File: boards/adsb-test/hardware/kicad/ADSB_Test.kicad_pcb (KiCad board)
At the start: 4 copper layers, 180.9 x 116 mm, 500 parts, among them J1001 Dev USB-C, J1101 USB-A (SDR hub), J1201 SMA GNSS (active antenna), J1301 LCD FPC 30p 0.5mm, J1302 Touch FPC 6p 0.5mm, J1401 m1421 JTAG (J-Link), J1402 ADSBee 1421 Dev Kit, J1403 SMA 1090/978, J1501 microSD (push-pull, detect), J1601 Kingst LA5016 (2x20 keyed), J1801 RP2040 GPIO (pins DNP), J1802 RP2040 SWD, J301 2S Li-ion pack (BAT+, GND, NT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, J601 U.FL Wi-Fi (from module IPEX), J602 RP-SMA Wi-Fi 2.4/5 GHz, J801 HR911105A, J901 User USB-C (PD sink + UART), Q1501 AO3401A, Q1701 MMBT3904, Q1702 MMBT3904, Q1703 MMBT3904, Q1704 MMBT3904, Q201 FDS9435A, SW1801 BOOTSEL (programmer), SW401 POWER (slide), SW601 BOOT, SW602 RESET, SW603 SLEEP/WAKE, U1001 USBLC6-2SC6, U1002 AP2112K-3.3, U1003 USB2514B, U1101 TPS259621DDA, U1102 USBLC6-2SC6, U1201 MAX-M10S, U1301 AP3012KTR-E1, U1302 AP2112K-1.8, U1303 AP3032KTR-G1, U1401 ADSBee m1421, U1402 74LVC1G97 (AND), U1403 74LVC1G32, U1404 74LVC1G07, U1405 SCN-2-11+, U1501 TCA6408APW, U1701 FT2232HL, U1702 93LC56B, U1703 74LVC1G07, U1704 74LVC1G125, U1705 74LVC1G07, U1706 74LVC1G125, U1801 RP2040, U1802 W25Q16JVSS, U1803 74LVC1G125, U1804 74LVC1G125, U1805 74LVC1G125, U1806 74LVC1G125, U201 STUSB4500QTR, U301 BQ25798, U302 MCP1703 3.0V (2 uA Iq), U411 TPS62933, U421 TPS62933, U430 TPS22917, U431 TPS22917, U432 TPS22917, U433 TPS22917, U501 PAC1954 (PM1), U502 PAC1954 (PM2), U503 PAC1954 (PM3), U601 ESP32-P4C5 Core (OSPTEK), U701 DS3231M, U801 LAN8720A, U901 CP2102N-A02-GQFN24, U902 USBLC6-2SC6, Y1001 24MHz, Y1701 12MHz, Y1801 12MHz, Y601 32.768kHz, Y801 25MHz

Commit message: ADSB_Test: board enlarged to 204.9 x 140 mm (20 mm border) for hand soldering
- gen_pcb.py: GAP = 20; panel-tied parts placed from the panel corner,
  edge parts from their edge; PCB regenerated (DRC clean, parity 0).
- floorplan.py: hand-solder factor 2.4, zones relative to the panel;
  every zone under 90 %, 62 % overall.
- Q28 answered; floorplan.md, architecture.md updated.

Co-Authored-By: Claude Opus 5.5 <noreply@anthropic.com>
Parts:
- J1101: footprint Connector_USB:USB_A_Molex_67643_Horizontal -> Connector_USB:USB_A_Wuerth_614004134726_Horizontal
- moved H1603 33.9 mm to (300.9, 236.0)
- moved J1201 33.9 mm to (302.8, 227.9)
- moved SH1201 33.9 mm to (284.0, 218.0)
- moved U1201 33.9 mm to (284.0, 218.0)
- moved J1601 26.8 mm to (173.8, 227.2)
- moved J1401 24.1 mm to (274.0, 156.0)
- moved SH1401 24.1 mm to (282.0, 132.0)
- moved U1401 24.1 mm to (282.0, 132.2)
- moved J1402 24.0 mm to (264.0, 107.7)
- moved BT301 24.0 mm to (328.1, 107.4)
- moved C1001 24.0 mm to (321.8, 182.1)
- moved C1002 24.0 mm to (327.7, 182.2)
- moved C1003 24.0 mm to (333.6, 182.1)
- moved C1004 24.0 mm to (338.9, 182.1)
- moved C1005 24.0 mm to (344.2, 182.1)
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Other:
- board size 180.9 x 116 mm -> 204.9 x 140 mm

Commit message: ADSB_Test PCB: A2 page with the board centred, key parts placed in their zones
gen_pcb.py packs ICs, connectors, switches, crystals and LEDs (55 parts)
into their floorplan zones with 2.5 mm between courtyards; passives and test
pads parked by sheet either side of the board. DRC parity 0.

Co-Authored-By: Claude Opus 5.5 <noreply@anthropic.com>
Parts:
- moved U901 247.1 mm to (242.9, 153.4)
- moved U1101 230.2 mm to (234.6, 195.0)
- moved U1102 227.5 mm to (245.2, 193.6)
- moved D902 226.0 mm to (221.7, 158.2)
- moved D901 222.7 mm to (229.2, 142.2)
- moved U902 220.1 mm to (222.2, 143.1)
- moved R1409 212.4 mm to (470.0, 180.9)
- moved TP1401 212.4 mm to (474.7, 181.2)
- moved TP1402 212.4 mm to (478.7, 181.2)
- moved U1501 211.6 mm to (223.7, 260.0)
- moved U1405 204.4 mm to (386.0, 143.0)
- moved U1404 204.2 mm to (379.1, 143.1)
- moved R1809 194.8 mm to (466.9, 94.0)
- moved R1810 194.8 mm to (472.2, 94.0)
- moved R1811 194.8 mm to (477.4, 94.0)
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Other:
- board text added: "[Charger Battery] 37 parts"
- board text added: "[Dev UARTs] 31 parts"
- board text added: "[Dev USB Hub] 27 parts"
- board text added: "[Dev m1421 Programmer] 31 parts"
- board text added: "[Display Touch] 60 parts"
- board text added: "[Ethernet] 29 parts"
- board text added: "[GPS] 12 parts"
- board text added: "[M1421] 24 parts"
- board text added: "[MCU Module] 29 parts"
- board text added: "[Power Input] 14 parts"
- board text added: "[Power Monitor] 7 parts"
- board text added: "[Power Rails] 50 parts"
- board text added: "[RTC] 4 parts"
- board text added: "[Storage Misc] 18 parts"
- board text added: "[USB Host] 10 parts"
- board text added: "[User USB-C] 9 parts"
- board text removed: "[Charger Battery] 41 parts"
- board text removed: "[Dev UARTs] 38 parts"
- board text removed: "[Dev USB Hub] 31 parts"
- board text removed: "[Dev m1421 Programmer] 40 parts"
- board text removed: "[Display Touch] 63 parts"
- board text removed: "[Ethernet] 31 parts"
- board text removed: "[GPS] 13 parts"
- board text removed: "[M1421] 30 parts"
- board text removed: "[MCU Module] 30 parts"
- board text removed: "[Power Input] 15 parts"
- board text removed: "[Power Monitor] 10 parts"
- board text removed: "[Power Rails] 56 parts"
- board text removed: "[RTC] 5 parts"
- board text removed: "[Storage Misc] 19 parts"
- board text removed: "[USB Host] 12 parts"
- board text removed: "[User USB-C] 13 parts"

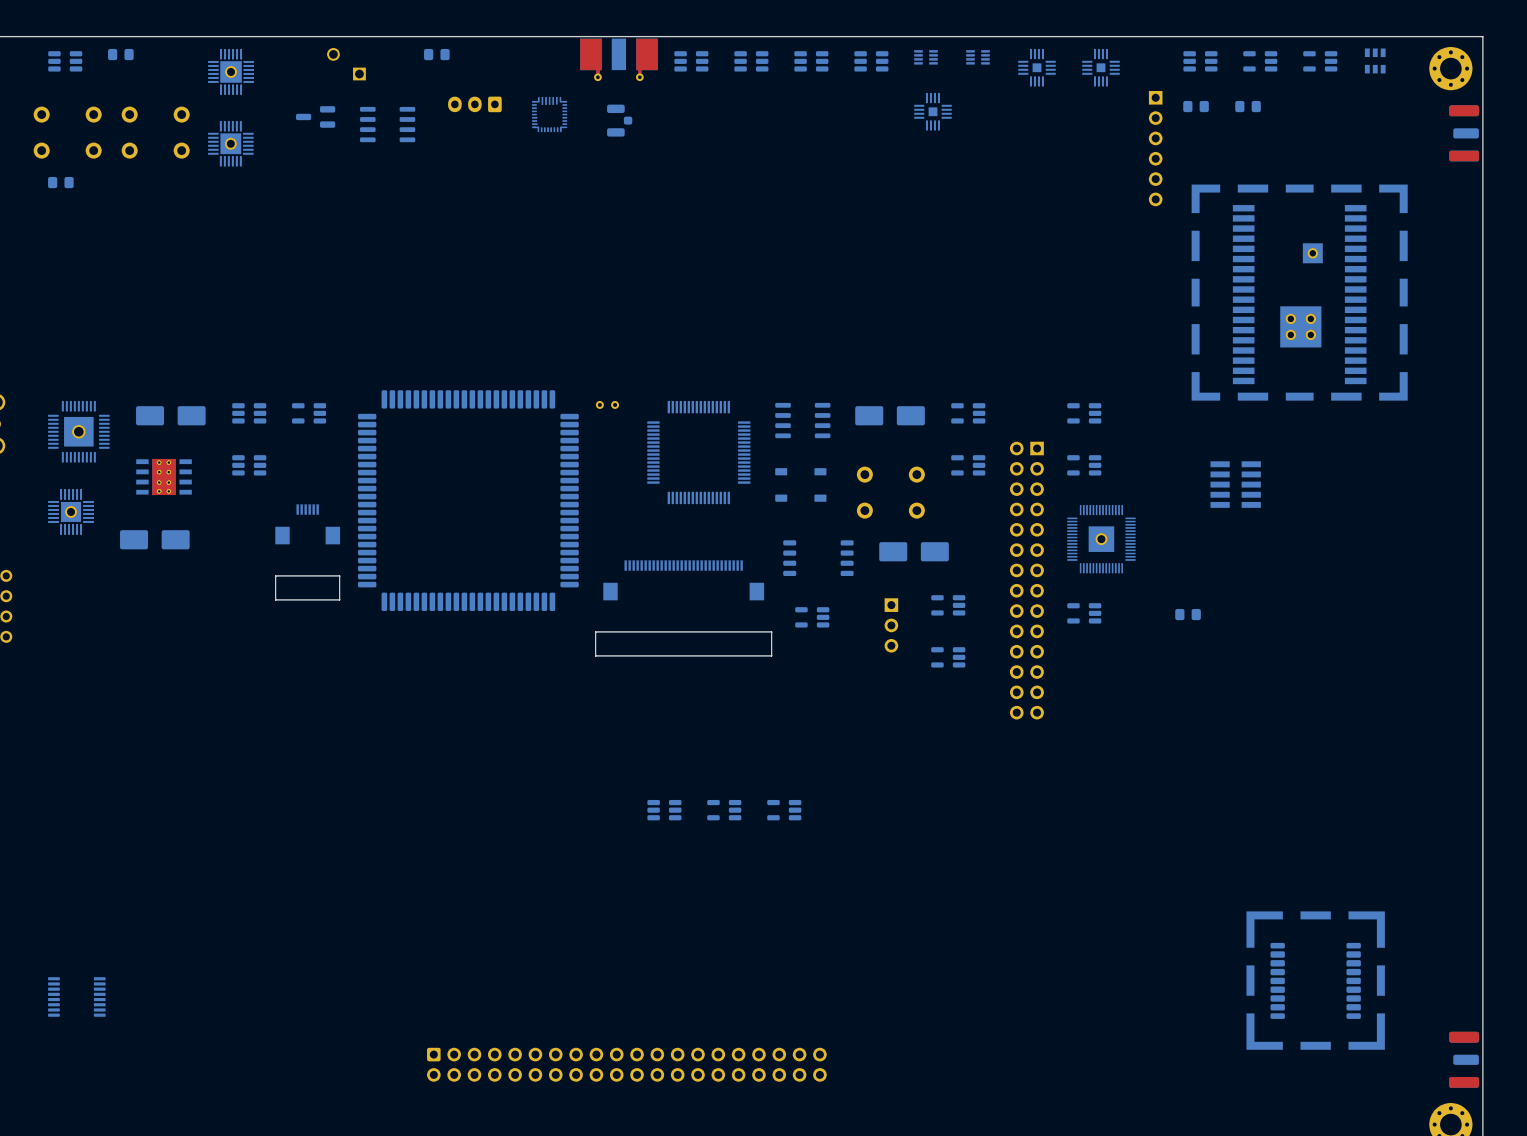
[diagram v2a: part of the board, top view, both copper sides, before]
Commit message: ADSB_Test gen_pcb: per-page PLACE arrays at the top, dump_placement.py
- All placement arrays at the top of gen_pcb.py; new PLACE dict with one
  list per schematic page ('REF', bx, by, rotation): uncommented = placed,
  commented = parked. Seeded from the board (55 placed, 415 parked).
- dump_placement.py --write refreshes PLACE from the saved PCB.
- Zone packer optional (AUTO_ZONES); grid/aux origin at the bottom-view
  board corner. Round trip reproduces every position.
- Keeps the user's EDGE_LEFT spacing and J1402 position.

Co-Authored-By: Claude Opus 5.5 <noreply@anthropic.com>
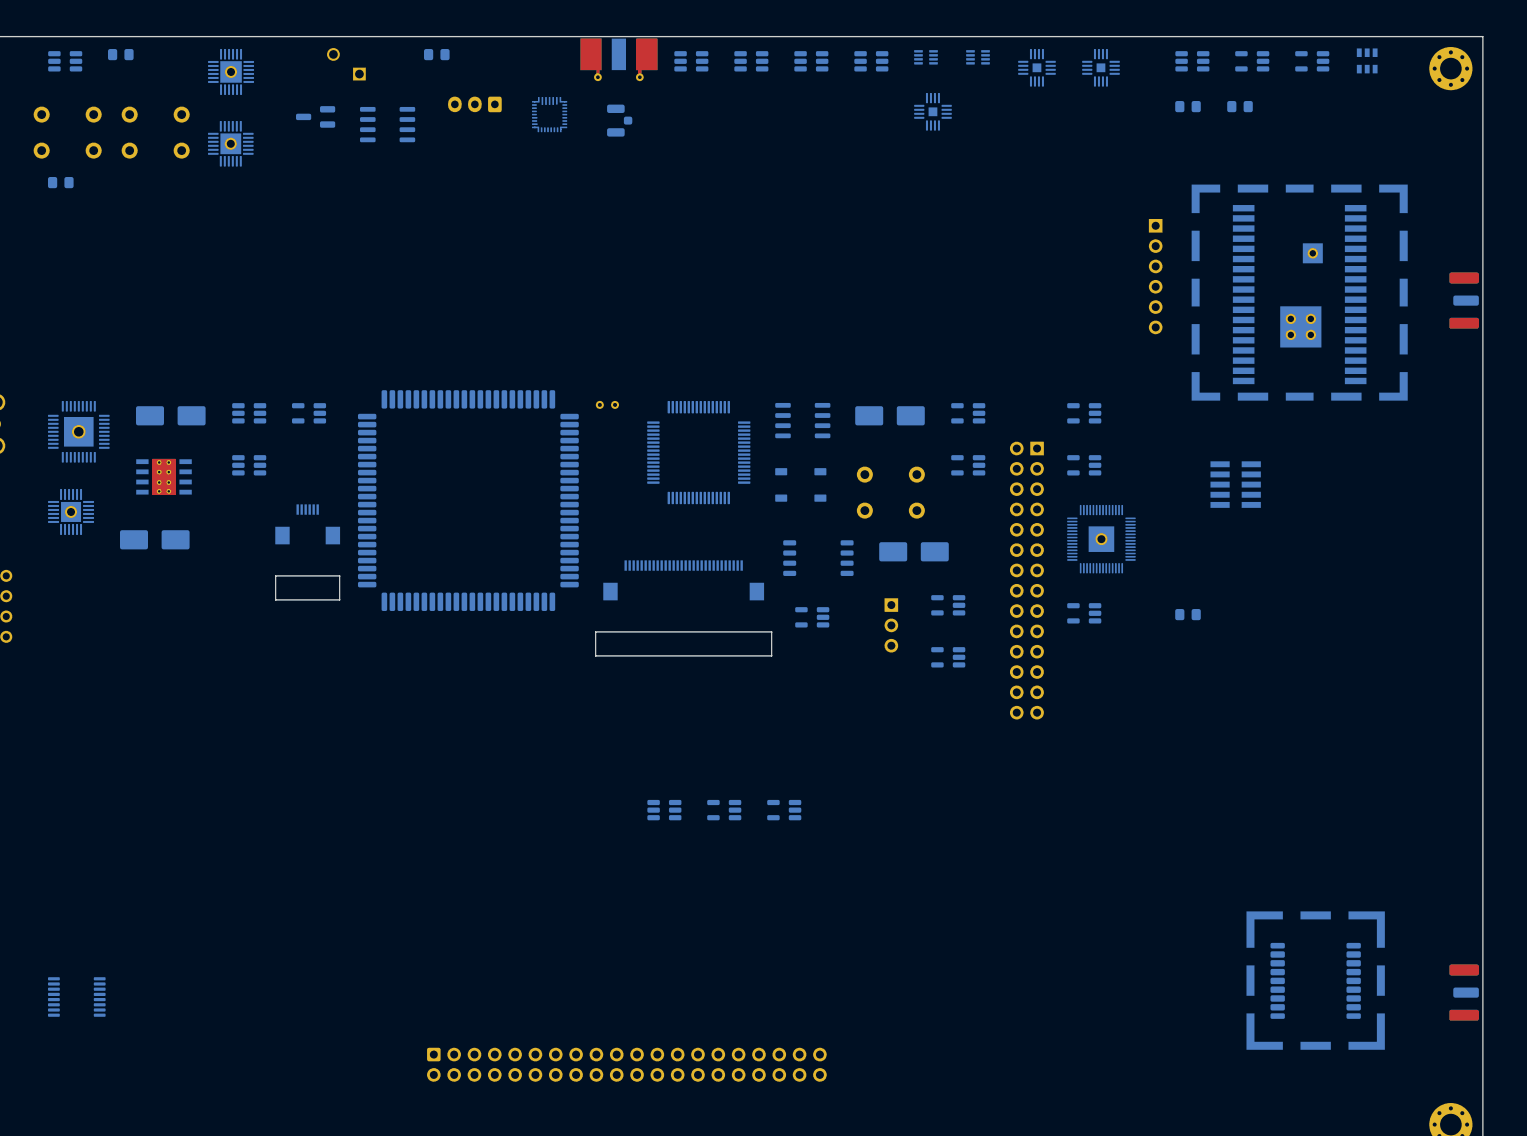
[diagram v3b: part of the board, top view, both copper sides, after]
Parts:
- moved J1403 20.9 mm to (397.4, 173.0)
- moved J1402 16.0 mm to (358.6, 163.7)
- moved J1201 8.40 mm to (397.4, 259.5)
- moved D1401 1.01 mm to (362.6, 148.8)
- moved D1402 1.01 mm to (369.1, 148.8)
- moved U1402 1.01 mm to (363.1, 143.1)
- moved U1403 1.01 mm to (370.6, 143.1)
- moved U1404 1.01 mm to (378.1, 143.1)
- moved U1405 1.01 mm to (385.0, 143.0)
